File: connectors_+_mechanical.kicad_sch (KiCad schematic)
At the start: 52 parts, among them J1 Motor0, J10 USB_C_Receptacle_USB2.0_14P, J2 Motor1, J3 Battery Input, J5 Conn_01x04, J6 Conn_01x04, Q1 BSP613P, U7 INA180A1

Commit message: Layout updates
Added 3v3 switcher layout + extras
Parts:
- R31: footprint Resistor_SMD:R_0402_1005Metric -> Resistor_SMD:R_1206_3216Metric
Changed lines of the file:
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@@
 			)
 		)
-		(property "Footprint" "Resistor_SMD:R_0402_1005Metric"
+		(property "Footprint" "Resistor_SMD:R_1206_3216Metric"
 			(at 132.08 129.54 0)
 			(effects

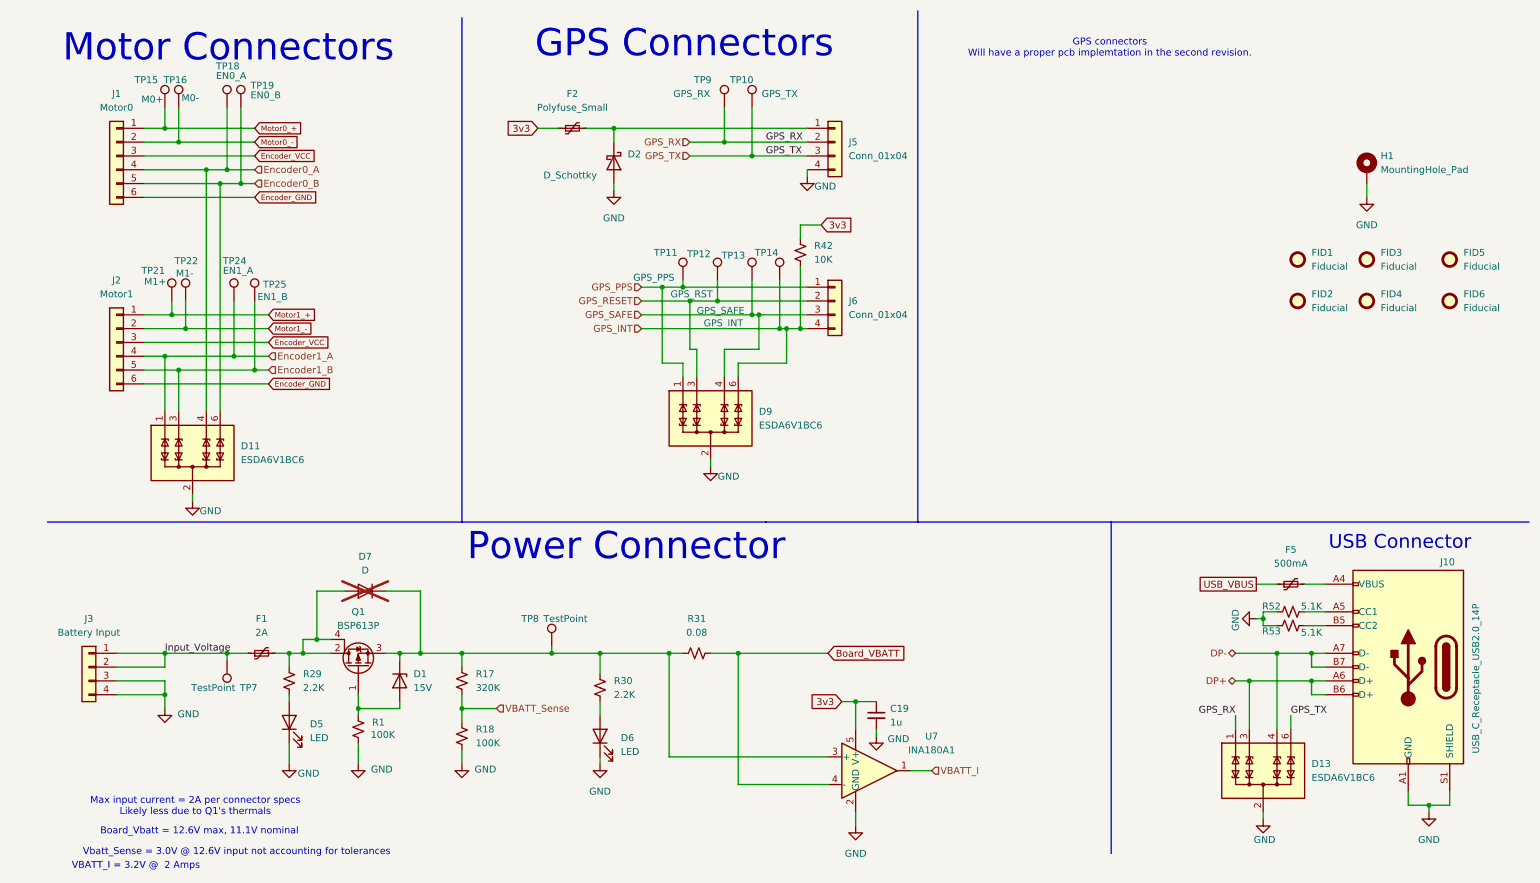
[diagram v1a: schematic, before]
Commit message: Updates
Routing updates, placed expansion connector.
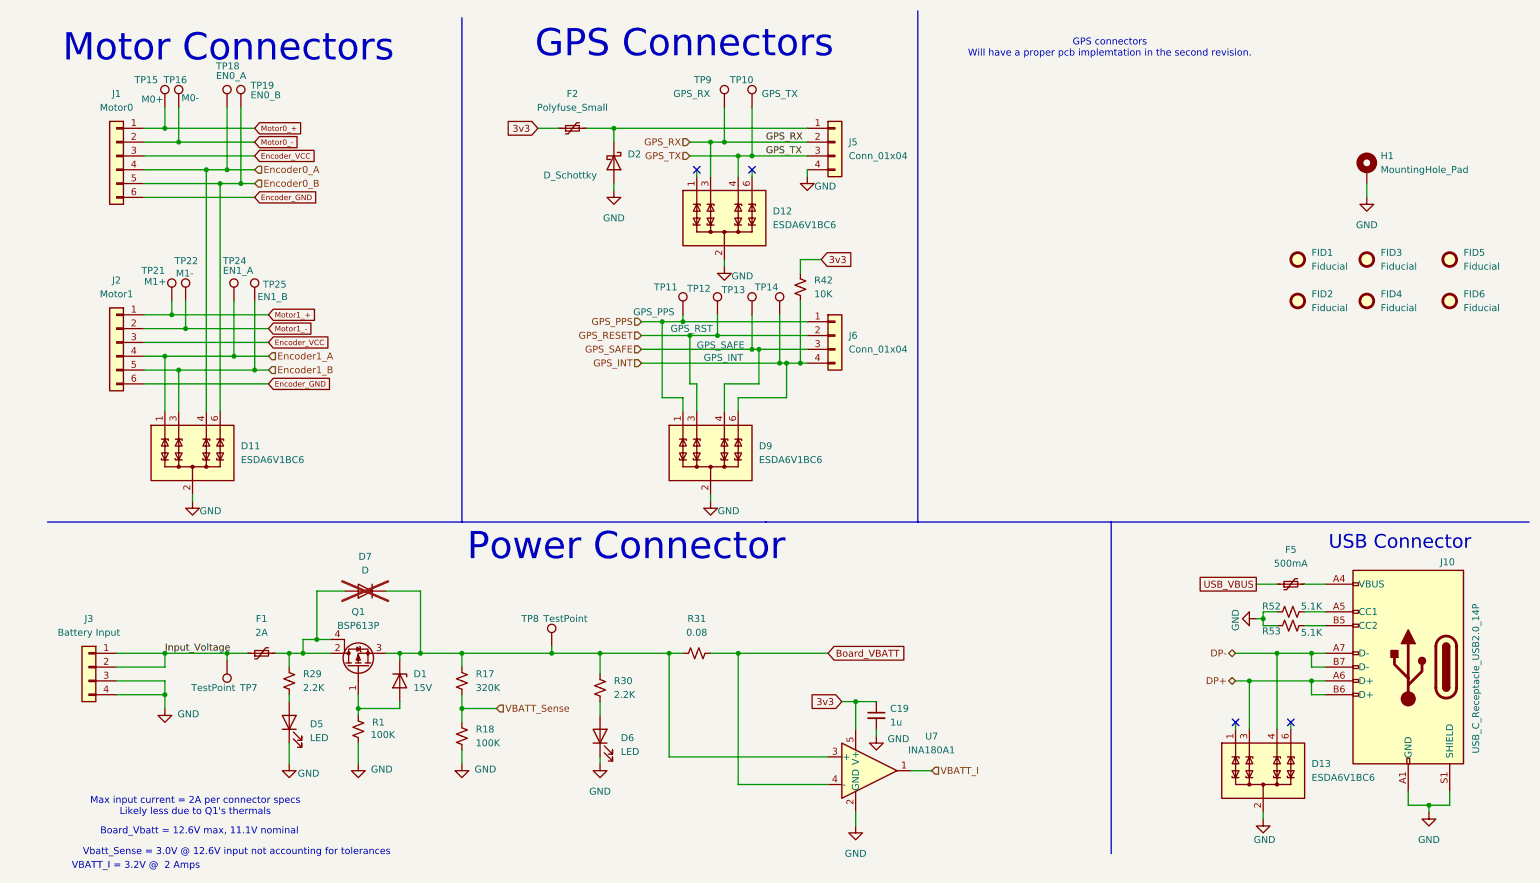
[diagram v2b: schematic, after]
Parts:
- added D12: ESDA6V1BC6, Package_TO_SOT_SMD:SOT-23-6, symbol Power_Protection:ESDA6V1BC6
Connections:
- net GND: now also D12.2 (COM), D12.5 (COM)
- net GPS_RX: now also D12.3 (TVS2); no longer D13.1 (TVS1)
- net GPS_TX: now also D12.4 (TVS3); no longer D13.6 (TVS4)
- no-connect marks 0 -> 4
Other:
- moved on the sheet: D9, J6, R42, TP11, TP12, TP13, TP14

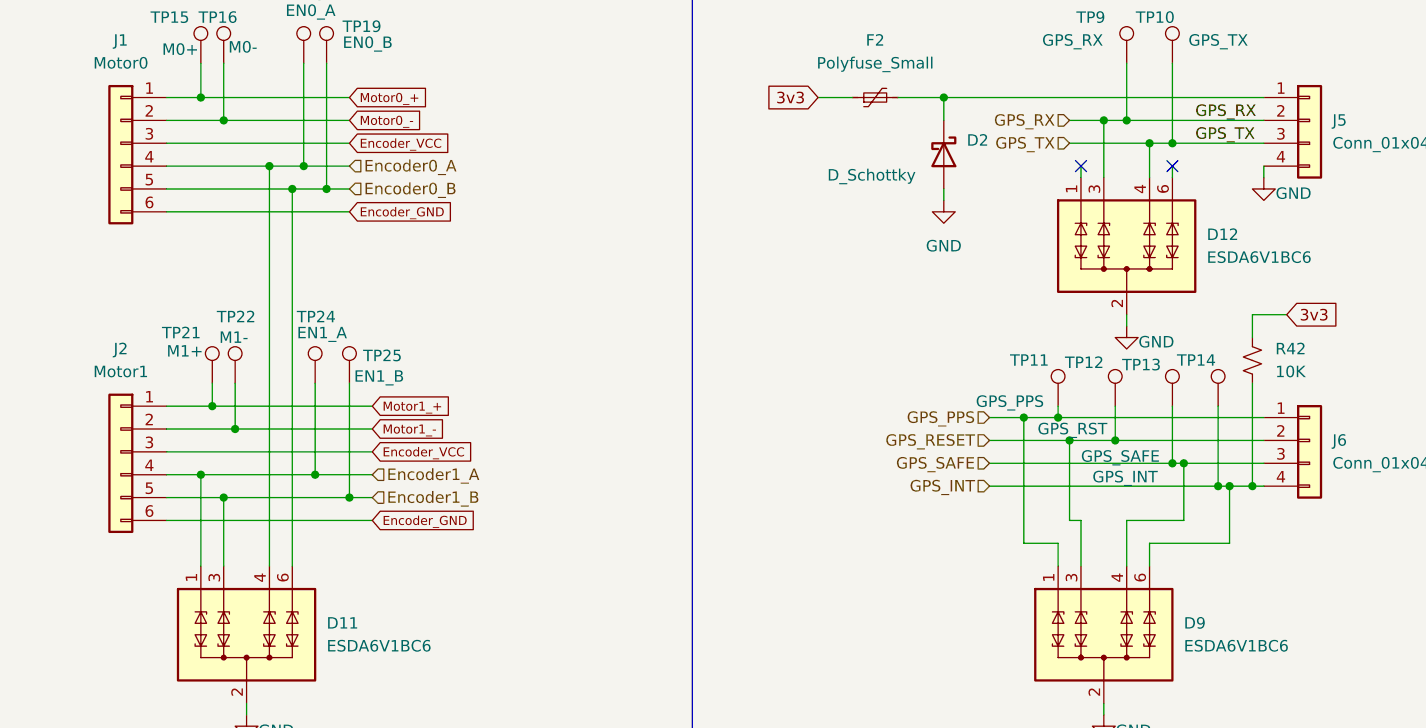
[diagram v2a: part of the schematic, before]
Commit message: layout updates
Updated encoder, esd and other layouts
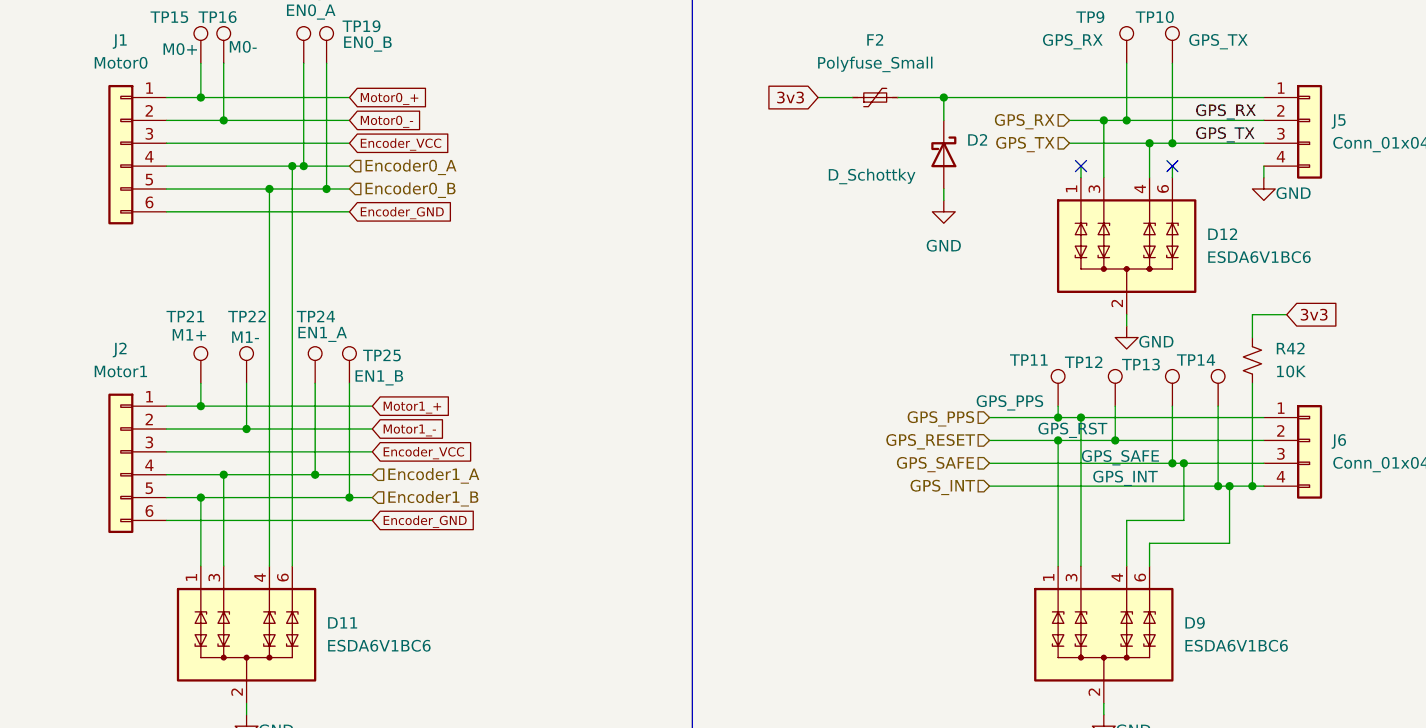
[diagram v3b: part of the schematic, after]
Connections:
- net Encoder0_A: now also D11.6 (TVS4); no longer D11.4 (TVS3)
- net Encoder0_B: now also D11.4 (TVS3); no longer D11.6 (TVS4)
- net Encoder1_A: now also D11.3 (TVS2); no longer D11.1 (TVS1)
- net Encoder1_B: now also D11.1 (TVS1); no longer D11.3 (TVS2)
- net GPS_PPS: now also D9.3 (TVS2); no longer D9.1 (TVS1)
- net GPS_RESET: now also D9.1 (TVS1); no longer D9.3 (TVS2)
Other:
- moved on the sheet: TP21, TP22

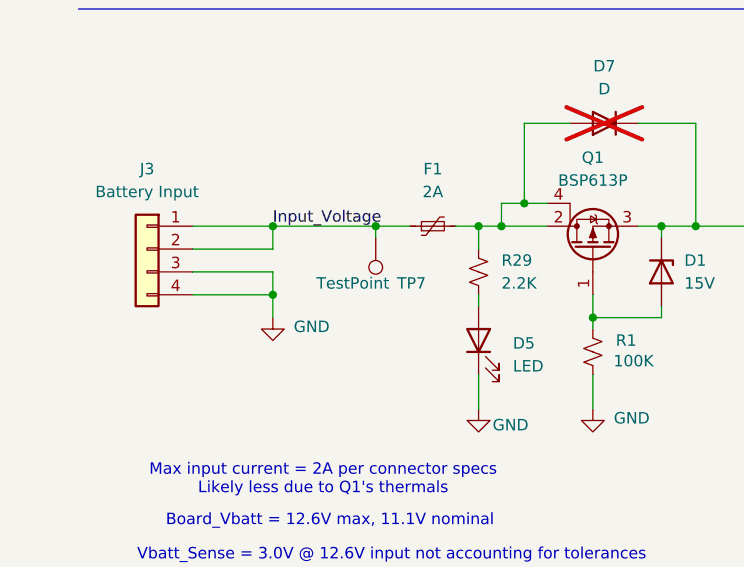
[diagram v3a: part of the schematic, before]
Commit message: Layout updates
testpoints, usb power, etc.
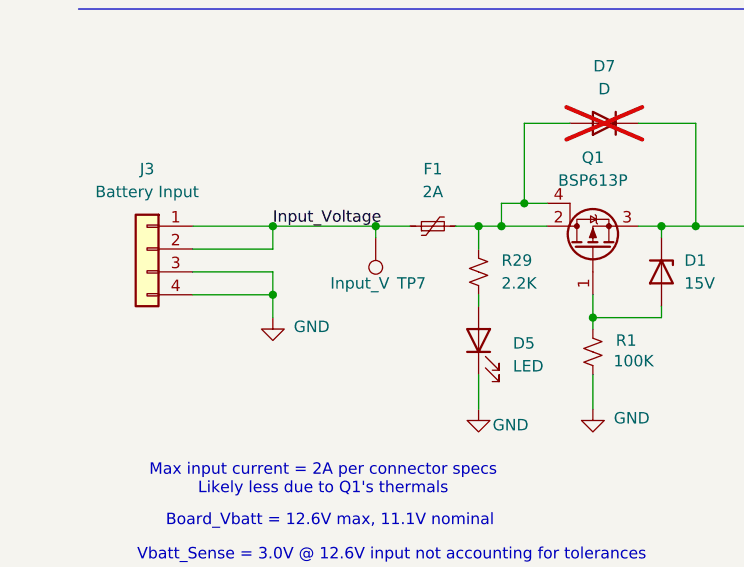
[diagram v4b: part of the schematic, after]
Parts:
- TP10, TP11, TP12, TP13, TP14, TP15, TP16, TP18, TP19, TP21, TP22, TP24, TP25, TP8, TP9: footprint TestPoint:TestPoint_Pad_1.0x1.0mm -> TestPoint:TestPoint_Pad_D1.0mm
- TP7: value TestPoint -> Input_V; footprint TestPoint:TestPoint_Pad_1.0x1.0mm -> TestPoint:TestPoint_Pad_D1.0mm
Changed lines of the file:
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@@
 			)
 		)
-		(property "Footprint" "TestPoint:TestPoint_Pad_1.0x1.0mm"
+		(property "Footprint" "TestPoint:TestPoint_Pad_D1.0mm"
 			(at 39.37 64.77 0)
 			(effects
@@
 			)
 		)
-		(property "Footprint" "TestPoint:TestPoint_Pad_1.0x1.0mm"
+		(property "Footprint" "TestPoint:TestPoint_Pad_D1.0mm"
 			(at 55.88 64.77 0)
 			(effects
@@
 			)
 		)
-		(property "Footprint" "TestPoint:TestPoint_Pad_1.0x1.0mm"
+		(property "Footprint" "TestPoint:TestPoint_Pad_D1.0mm"
 			(at 53.34 29.21 0)
 			(effects
@@
 			)
 		)
-		(property "Footprint" "TestPoint:TestPoint_Pad_1.0x1.0mm"
+		(property "Footprint" "TestPoint:TestPoint_Pad_D1.0mm"
 			(at 44.45 64.77 0)
 			(effects
@@
 			)
 		)
-		(property "Footprint" "TestPoint:TestPoint_Pad_1.0x1.0mm"
+		(property "Footprint" "TestPoint:TestPoint_Pad_D1.0mm"
 			(at 142.24 29.21 0)
 			(effects
@@
 			)
 		)
-		(property "Footprint" "TestPoint:TestPoint_Pad_1.0x1.0mm"
+		(property "Footprint" "TestPoint:TestPoint_Pad_D1.0mm"
 			(at 50.8 29.21 0)
 			(effects
@@
 			)
 		)
-		(property "Footprint" "TestPoint:TestPoint_Pad_1.0x1.0mm"
+		(property "Footprint" "TestPoint:TestPoint_Pad_D1.0mm"
 			(at 134.62 67.31 0)
 			(effects
@@
 			)
 		)
-		(property "Footprint" "TestPoint:TestPoint_Pad_1.0x1.0mm"
+		(property "Footprint" "TestPoint:TestPoint_Pad_D1.0mm"
 			(at 39.37 29.21 0)
 			(effects
@@
 			)
 		)
-		(property "Footprint" "TestPoint:TestPoint_Pad_1.0x1.0mm"
+		(property "Footprint" "TestPoint:TestPoint_Pad_D1.0mm"
 			(at 110.49 128.27 0)
 			(effects
@@
 			)
 		)
-		(property "Footprint" "TestPoint:TestPoint_Pad_1.0x1.0mm"
+		(property "Footprint" "TestPoint:TestPoint_Pad_D1.0mm"
 			(at 147.32 67.31 0)
 			(effects
@@
 			)
 		)
-		(property "Footprint" "TestPoint:TestPoint_Pad_1.0x1.0mm"
+		(property "Footprint" "TestPoint:TestPoint_Pad_D1.0mm"
 			(at 41.91 29.21 0)
 			(effects
@@
 			)
 		)
-		(property "Footprint" "TestPoint:TestPoint_Pad_1.0x1.0mm"
+		(property "Footprint" "TestPoint:TestPoint_Pad_D1.0mm"
 			(at 52.07 64.77 0)
 			(effects
@@
 			)
 		)
-		(property "Value" "TestPoint"
+		(property "Value" "Input_V"
 			(at 47.244 135.89 0)
 			(effects
@@
 			)
 		)
-		(property "Footprint" "TestPoint:TestPoint_Pad_1.0x1.0mm"
+		(property "Footprint" "TestPoint:TestPoint_Pad_D1.0mm"
 			(at 40.64 130.81 0)
 			(effects
@@
 			)
 		)
-		(property "Footprint" "TestPoint:TestPoint_Pad_1.0x1.0mm"
+		(property "Footprint" "TestPoint:TestPoint_Pad_D1.0mm"
 			(at 147.32 29.21 0)
 			(effects
@@
 			)
 		)
-		(property "Footprint" "TestPoint:TestPoint_Pad_1.0x1.0mm"
+		(property "Footprint" "TestPoint:TestPoint_Pad_D1.0mm"
 			(at 152.4 67.31 0)
 			(effects
@@
 			)
 		)
-		(property "Footprint" "TestPoint:TestPoint_Pad_1.0x1.0mm"
+		(property "Footprint" "TestPoint:TestPoint_Pad_D1.0mm"
 			(at 140.97 67.31 0)
 			(effects

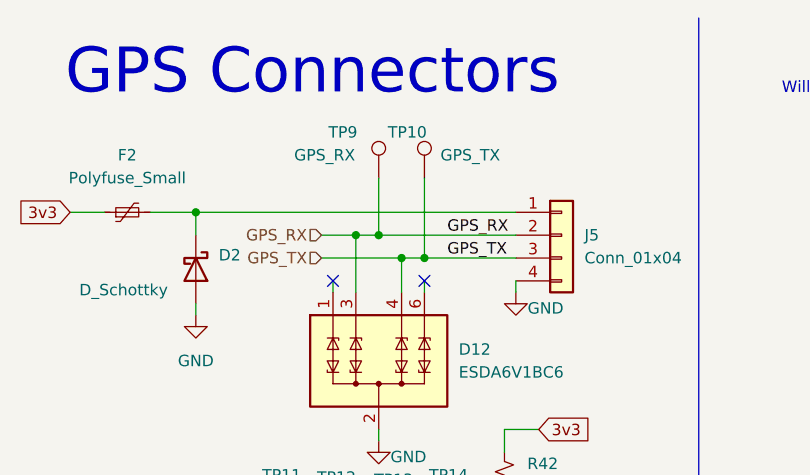
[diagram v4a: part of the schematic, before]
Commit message: layout updates
removes ADC 2 and ADC 3 connections for space reasons
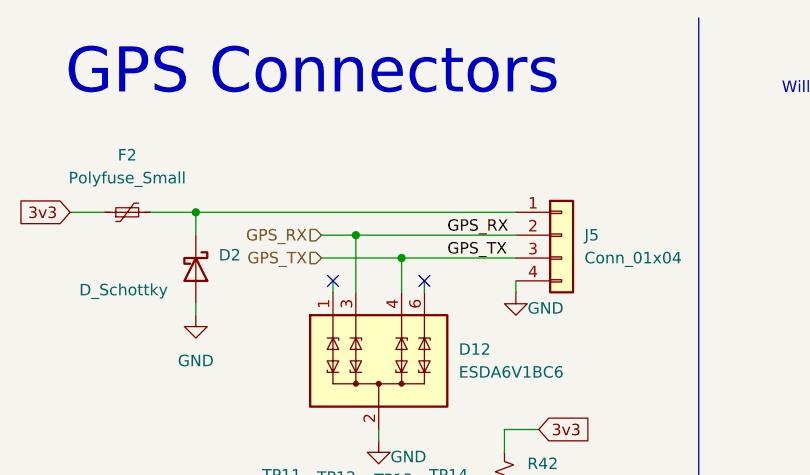
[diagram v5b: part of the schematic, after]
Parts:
- removed TP10: GPS_TX, TestPoint:TestPoint_Pad_D1.0mm, symbol Connector:TestPoint
- removed TP9: GPS_RX, TestPoint:TestPoint_Pad_D1.0mm, symbol Connector:TestPoint
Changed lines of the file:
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@@
 	)
 	(junction
-		(at 137.16 35.56)
-		(diameter 0)
-		(color 0 0 0 0)
-	)
-	(junction
 		(at 127 129.54)
 		(diameter 0)
@@
 	)
 	(junction
-		(at 142.24 38.1)
-		(diameter 0)
-		(color 0 0 0 0)
-	)
-	(junction
 		(at 161.29 138.43)
 		(diameter 0)
@@
 	(wire
 		(pts
-			(xy 142.24 29.21) (xy 142.24 38.1)
-		)
-		(stroke
-			(width 0)
-			(type default)
-		)
-	)
-	(wire
-		(pts
 			(xy 152.4 40.64) (xy 152.4 41.91)
 		)
@@
 	(wire
 		(pts
-			(xy 134.62 35.56) (xy 137.16 35.56)
+			(xy 134.62 35.56) (xy 152.4 35.56)
 		)
 		(stroke
@@
 	(wire
 		(pts
-			(xy 137.16 35.56) (xy 152.4 35.56)
-		)
-		(stroke
-			(width 0)
-			(type default)
-		)
-	)
-	(wire
-		(pts
 			(xy 77.47 129.54) (xy 77.47 130.81)
 		)
@@
 	(wire
 		(pts
-			(xy 142.24 38.1) (xy 152.4 38.1)
+			(xy 139.7 38.1) (xy 152.4 38.1)
 		)
 		(stroke
@@
 	(wire
 		(pts
-			(xy 137.16 29.21) (xy 137.16 35.56)
-		)
-		(stroke
-			(width 0)
-			(type default)
-		)
-	)
-	(wire
-		(pts
 			(xy 231.14 129.54) (xy 238.76 129.54)
 		)
@@
 	(wire
 		(pts
-			(xy 139.7 38.1) (xy 142.24 38.1)
-		)
-		(stroke
-			(width 0)
-			(type default)
-		)
-	)
-	(wire
-		(pts
 			(xy 88.9 139.7) (xy 88.9 142.24)
 		)
@@
 	)
 	(symbol
-		(lib_id "Connector:TestPoint")
-		(at 137.16 29.21 0)
-		(unit 1)
-		(exclude_from_sim no)
-		(in_bom yes)
-		(on_board yes)
-		(dnp no)
-		(property "Reference" "TP9"
-			(at 131.572 24.13 0)
-			(effects
-				(font
-					(size 1.27 1.27)
-				)
-				(justify left)
-			)
-		)
-		(property "Value" "GPS_RX"
-			(at 127.762 26.67 0)
-			(effects
-				(font
-					(size 1.27 1.27)
-				)
-				(justify left)
-			)
-		)
-		(property "Footprint" "TestPoint:TestPoint_Pad_D1.0mm"
-			(at 142.24 29.21 0)
-			(effects
-				(font
-					(size 1.27 1.27)
-				)
-				(hide yes)
-			)
-		)
-		(property "Datasheet" "~"
-			(at 142.24 29.21 0)
-			(effects
-				(font
-					(size 1.27 1.27)
-				)
-				(hide yes)
-			)
-		)
-		(property "Description" "test point"
-			(at 137.16 29.21 0)
-			(effects
-				(font
-					(size 1.27 1.27)
-				)
-				(hide yes)
-			)
-		)
-		(pin "1"
-		)
-		(instances
-			(project "moon_child"
-				(path "/9fe08eae-9310-46cf-b272-eac4209a7b3e/2020c3b7-5d3f-4410-b013-36b6a2638d7a"
-					(reference "TP9")
-					(unit 1)
-				)
-			)
-		)
-	)
-	(symbol
 		(lib_id "power:GND")
 		(at 114.3 149.86 0)
@@
 					(unit 1)
 				)
-			)
-		)
-	)
-	(symbol
-		(lib_id "Connector:TestPoint")
-		(at 142.24 29.21 0)
-		(unit 1)
-		(exclude_from_sim no)
-		(in_bom yes)
-		(on_board yes)
-		(dnp no)
-		(property "Reference" "TP10"
-			(at 138.176 24.13 0)
-			(effects
-				(font
-					(size 1.27 1.27)
-				)
-				(justify left)
-			)
-		)
-		(property "Value" "GPS_TX"
-			(at 144.018 26.67 0)
-			(effects
-				(font
-					(size 1.27 1.27)
-				)
-				(justify left)
-			)
-		)
-		(property "Footprint" "TestPoint:TestPoint_Pad_D1.0mm"
-			(at 147.32 29.21 0)
-			(effects
-				(font
-					(size 1.27 1.27)
-				)
-				(hide yes)
-			)
-		)
-		(property "Datasheet" "~"
-			(at 147.32 29.21 0)
-			(effects
-				(font
-					(size 1.27 1.27)
-				)
-				(hide yes)
-			)
-		)
-		(property "Description" "test point"
-			(at 142.24 29.21 0)
-			(effects
-				(font
-					(size 1.27 1.27)
-				)
-				(hide yes)
-			)
-		)
-		(pin "1"
-		)
-		(instances
-			(project "moon_child"
-				(path "/9fe08eae-9310-46cf-b272-eac4209a7b3e/2020c3b7-5d3f-4410-b013-36b6a2638d7a"
-					(reference "TP10")
-					(unit 1)
-				)
